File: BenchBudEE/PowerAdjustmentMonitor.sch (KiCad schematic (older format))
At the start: 0 parts

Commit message: Power Control Conditioning and monitoring block diagram
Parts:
- added JP? (x3): JUMPER, ~, symbol JUMPER
- added R? (x8): R, ~, symbol R
- added R? (x2): RVAR, ~, symbol RVAR
- added U? (x2): LM317, ~, symbol LM317
- added U? (x2): 7805, ~, symbol 7805
- added U? (x2): LM324, symbol LM324
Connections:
- net labels added: +12V, +3.3V, +5V, -12V, 3V3_MON, 5V_MON, AGND, FE_V+, FE_V-, GND, V+_ADJ, V+_ADJ_MON, V+_CURR_MON, V+_MON, V-_ADJ, V-_ADJ_MON, V-_CURR_MON, V-_MON
- wire segments 0 -> 74

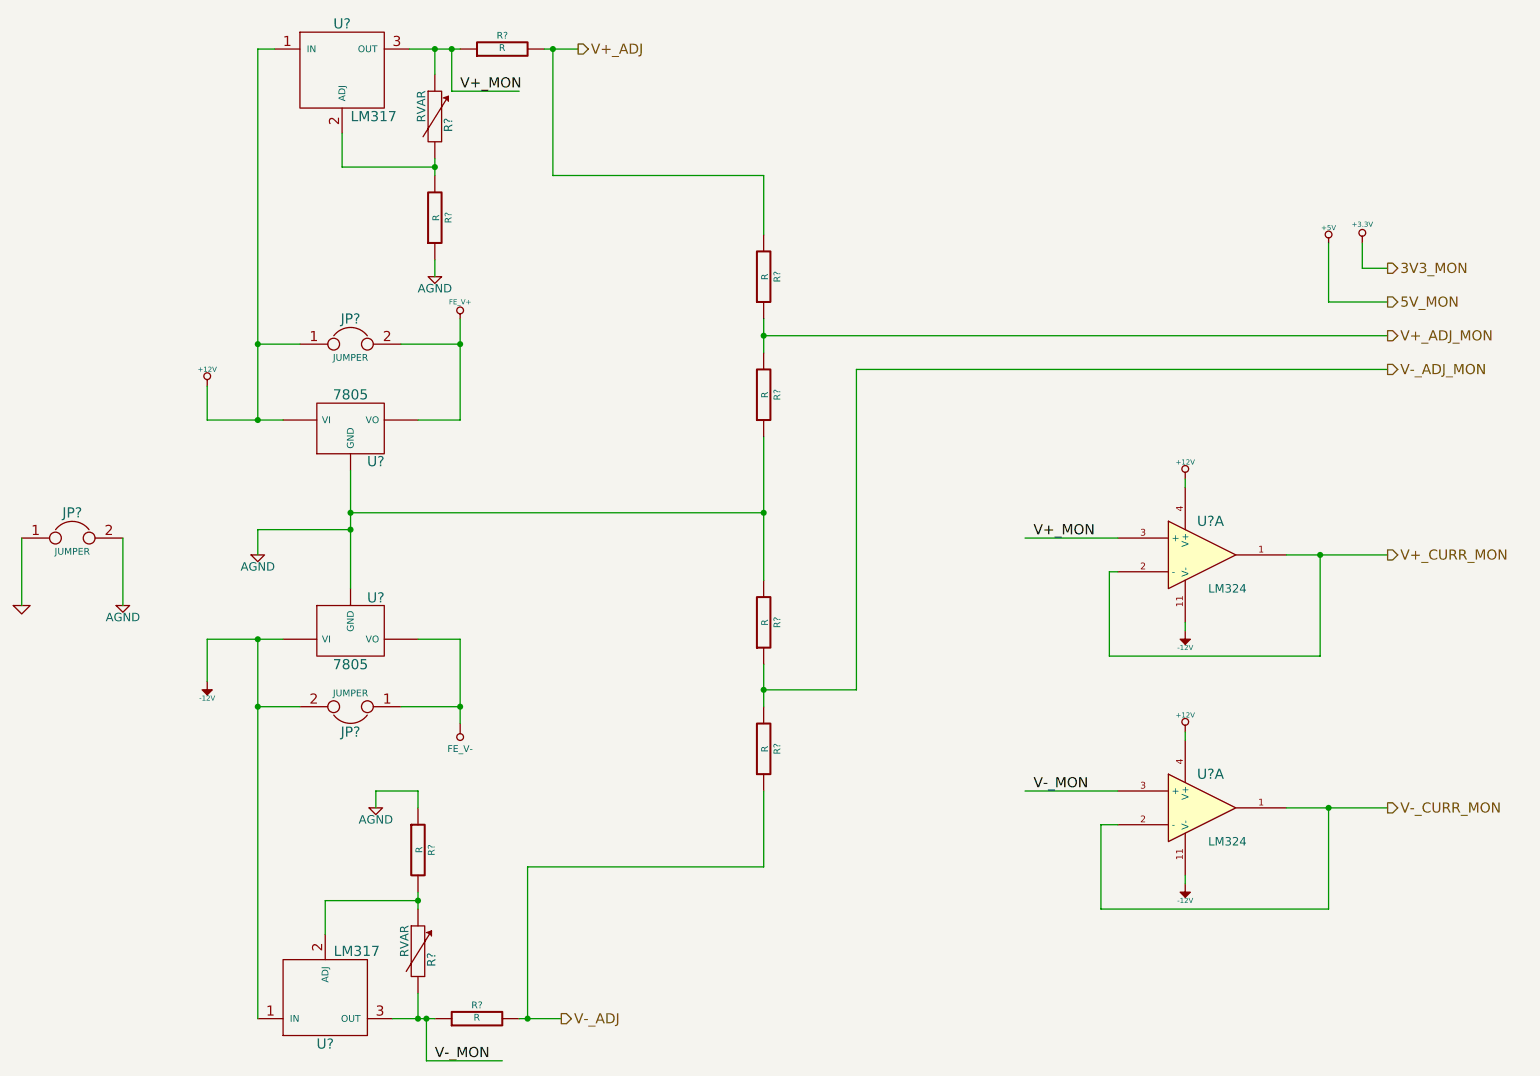
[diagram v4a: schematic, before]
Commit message: PCB Outline created and changes during  components choice
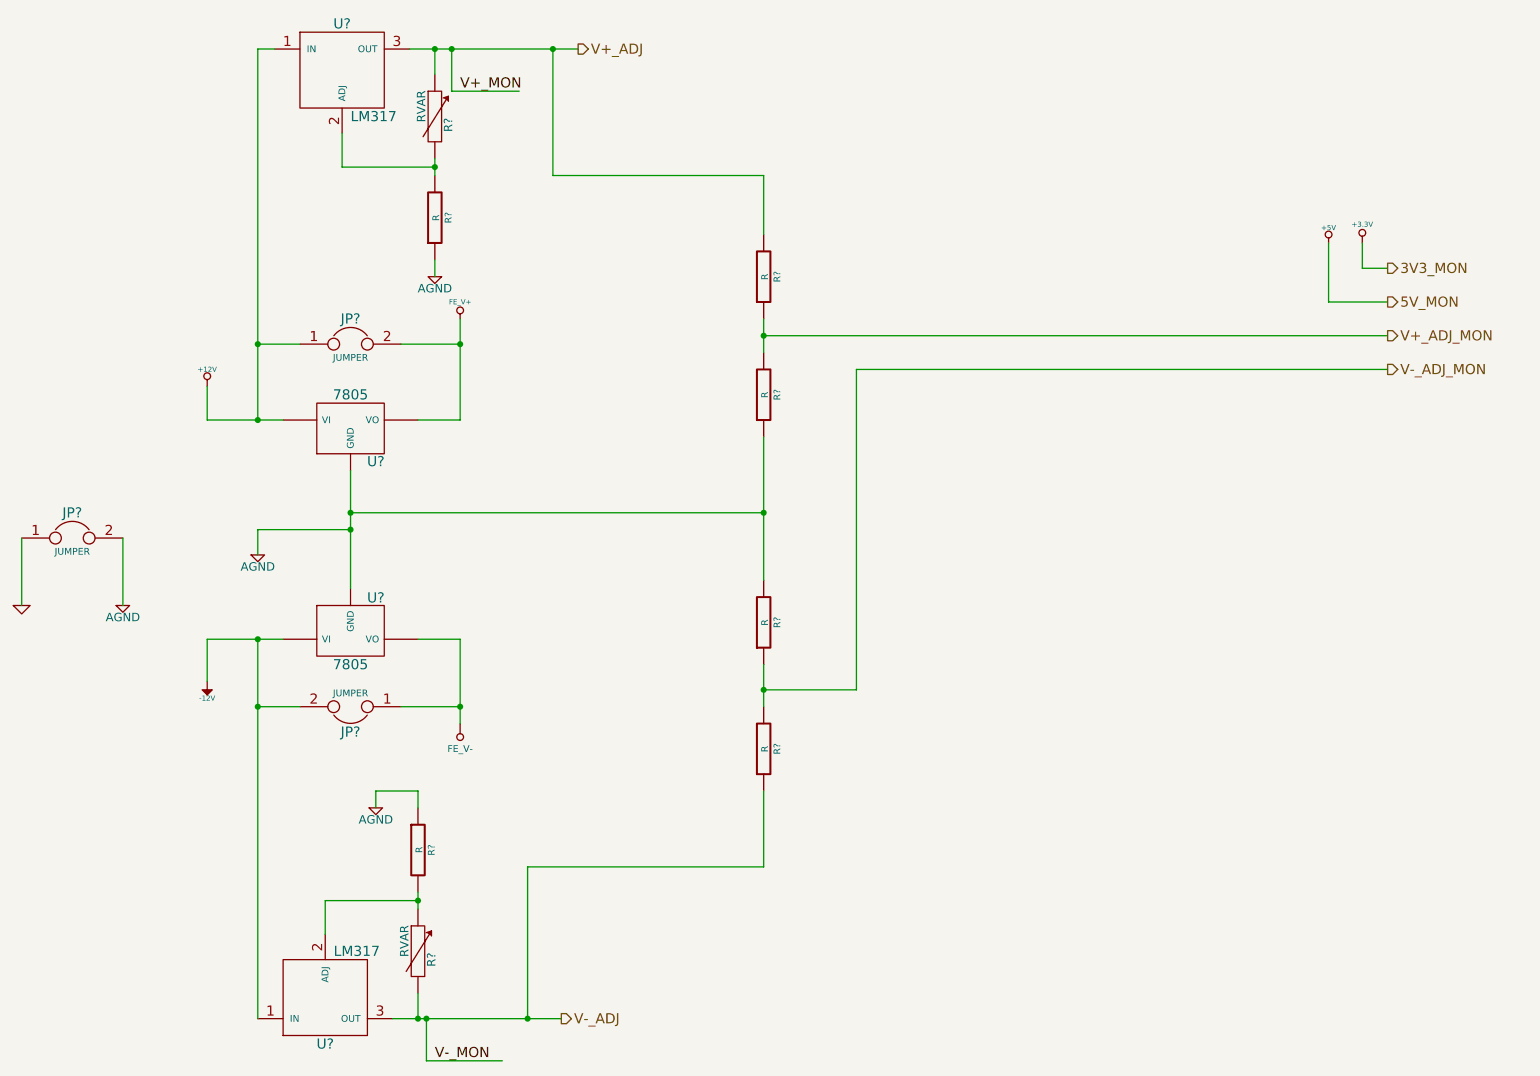
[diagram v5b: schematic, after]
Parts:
- removed R? (x2): R, ~, symbol R
- removed U? (x2): LM324, symbol LM324
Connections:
- net labels removed: V+_CURR_MON, V-_CURR_MON
- wire segments 74 -> 56
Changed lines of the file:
@@
 $Descr A4 11693 8268
 encoding utf-8
-Sheet 5 9
+Sheet 8 9
 Title ""
-Date "11 feb 2014"
+Date "16 feb 2014"
 Rev ""
 Comp ""
@@
 Text HLabel 8950 2800 2    60   Output ~ 0
 V-_ADJ_MON
-Text HLabel 8950 3900 2    60   Output ~ 0
-V+_CURR_MON
-Text HLabel 8950 5400 2    60   Output ~ 0
-V-_CURR_MON
 $Comp
 L R R?
@@
 Wire Wire Line
 	8800 2200 8950 2200
-$Comp
-L R R?
-U 1 1 52F7467B
-P 3550 6650
-F 0 "R?" V 3630 6650 40  0000 C CNN
-F 1 "R" V 3557 6651 40  0000 C CNN
-F 2 "~" V 3480 6650 30  0000 C CNN
-F 3 "~" H 3550 6650 30  0000 C CNN
-	1    3550 6650
-	0    -1   -1   0
-$EndComp
-Wire Wire Line
-	3050 6650 3300 6650
-Wire Wire Line
-	3800 6650 4050 6650
-$Comp
-L R R?
-U 1 1 52F74710
-P 3700 900
-F 0 "R?" V 3780 900 40  0000 C CNN
-F 1 "R" V 3707 901 40  0000 C CNN
-F 2 "~" V 3630 900 30  0000 C CNN
-F 3 "~" H 3700 900 30  0000 C CNN
-	1    3700 900
-	0    -1   -1   0
-$EndComp
-Wire Wire Line
-	3150 900  3450 900
-Wire Wire Line
-	3950 900  4150 900
+Wire Wire Line
+	3050 6650 4050 6650
+Wire Wire Line
+	3150 900  4150 900
 Wire Wire Line
 	3400 900  3400 1150
@@
 	5800 2800 8950 2800
 $Comp
-L LM324 U?
-U 1 1 52F74E00
-P 7850 3900
-F 0 "U?" H 7900 4100 60  0000 C CNN
-F 1 "LM324" H 8000 3700 50  0000 C CNN
-F 2 "" H 7850 3900 60  0000 C CNN
-F 3 "" H 7850 3900 60  0000 C CNN
-	1    7850 3900
-	1    0    0    -1
-$EndComp
-$Comp
-L -12V #PWR?
-U 1 1 52F74E13
-P 7750 4350
-F 0 "#PWR?" H 7750 4480 20  0001 C CNN
-F 1 "-12V" H 7750 4450 30  0000 C CNN
-F 2 "" H 7750 4350 60  0000 C CNN
-F 3 "" H 7750 4350 60  0000 C CNN
-	1    7750 4350
-	-1   0    0    1
-$EndComp
-Wire Wire Line
-	7750 4300 7750 4350
-$Comp
-L +12V #PWR?
-U 1 1 52F74E71
-P 7750 3450
-F 0 "#PWR?" H 7750 3400 20  0001 C CNN
-F 1 "+12V" H 7750 3550 30  0000 C CNN
-F 2 "" H 7750 3450 60  0000 C CNN
-F 3 "" H 7750 3450 60  0000 C CNN
-	1    7750 3450
-	1    0    0    -1
-$EndComp
-Wire Wire Line
-	7750 3500 7750 3450
-$Comp
-L LM324 U?
-U 1 1 52F74EC6
-P 7850 5400
-F 0 "U?" H 7900 5600 60  0000 C CNN
-F 1 "LM324" H 8000 5200 50  0000 C CNN
-F 2 "" H 7850 5400 60  0000 C CNN
-F 3 "" H 7850 5400 60  0000 C CNN
-	1    7850 5400
-	1    0    0    -1
-$EndComp
-$Comp
-L -12V #PWR?
-U 1 1 52F74ECC
-P 7750 5850
-F 0 "#PWR?" H 7750 5980 20  0001 C CNN
-F 1 "-12V" H 7750 5950 30  0000 C CNN
-F 2 "" H 7750 5850 60  0000 C CNN
-F 3 "" H 7750 5850 60  0000 C CNN
-	1    7750 5850
-	-1   0    0    1
-$EndComp
-Wire Wire Line
-	7750 5800 7750 5850
-$Comp
-L +12V #PWR?
-U 1 1 52F74ED3
-P 7750 4950
-F 0 "#PWR?" H 7750 4900 20  0001 C CNN
-F 1 "+12V" H 7750 5050 30  0000 C CNN
-F 2 "" H 7750 4950 60  0000 C CNN
-F 3 "" H 7750 4950 60  0000 C CNN
-	1    7750 4950
-	1    0    0    -1
-$EndComp
-Wire Wire Line
-	7750 5000 7750 4950
-Wire Wire Line
-	8350 5400 8950 5400
-Wire Wire Line
-	8350 3900 8950 3900
-Wire Wire Line
-	7350 4000 7300 4000
-Wire Wire Line
-	7300 4000 7300 4500
-Wire Wire Line
-	7300 4500 8550 4500
-Wire Wire Line
-	8550 4500 8550 3900
-Connection ~ 8550 3900
-Wire Wire Line
-	7350 5500 7250 5500
-Wire Wire Line
-	7250 5500 7250 6000
-Wire Wire Line
-	7250 6000 8600 6000
-Wire Wire Line
-	8600 6000 8600 5400
-Connection ~ 8600 5400
-Text Label 6850 5300 0    60   ~ 0
-V-_MON
-Text Label 6850 3800 0    60   ~ 0
-V+_MON
-Wire Wire Line
-	6800 3800 7350 3800
-Wire Wire Line
-	7350 5300 6800 5300
-$Comp
 L RVAR R?
